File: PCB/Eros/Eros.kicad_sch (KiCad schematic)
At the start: 113 parts, among them IC1 ADS1292RIPBS, J1 USB_C_PowerOnly_6P, J2 UART, J3 Li-ion, J4 Conn_01x08_Socket, J5 AudioJack3, J6 Micro_SD_Card, J7 Conn_01x03_Socket, Q1 BC817, SW1 SW_Push, SW2 SW_Push, SW4 SW_Push, SW5 SW_Push, SW6 SW_SPDT, U1 ESP32-WROOM-32E, U2 LIS3DH, U3 MCP73831-2-OT, U4 AP2112K-3.3, U6 MCP100-315D

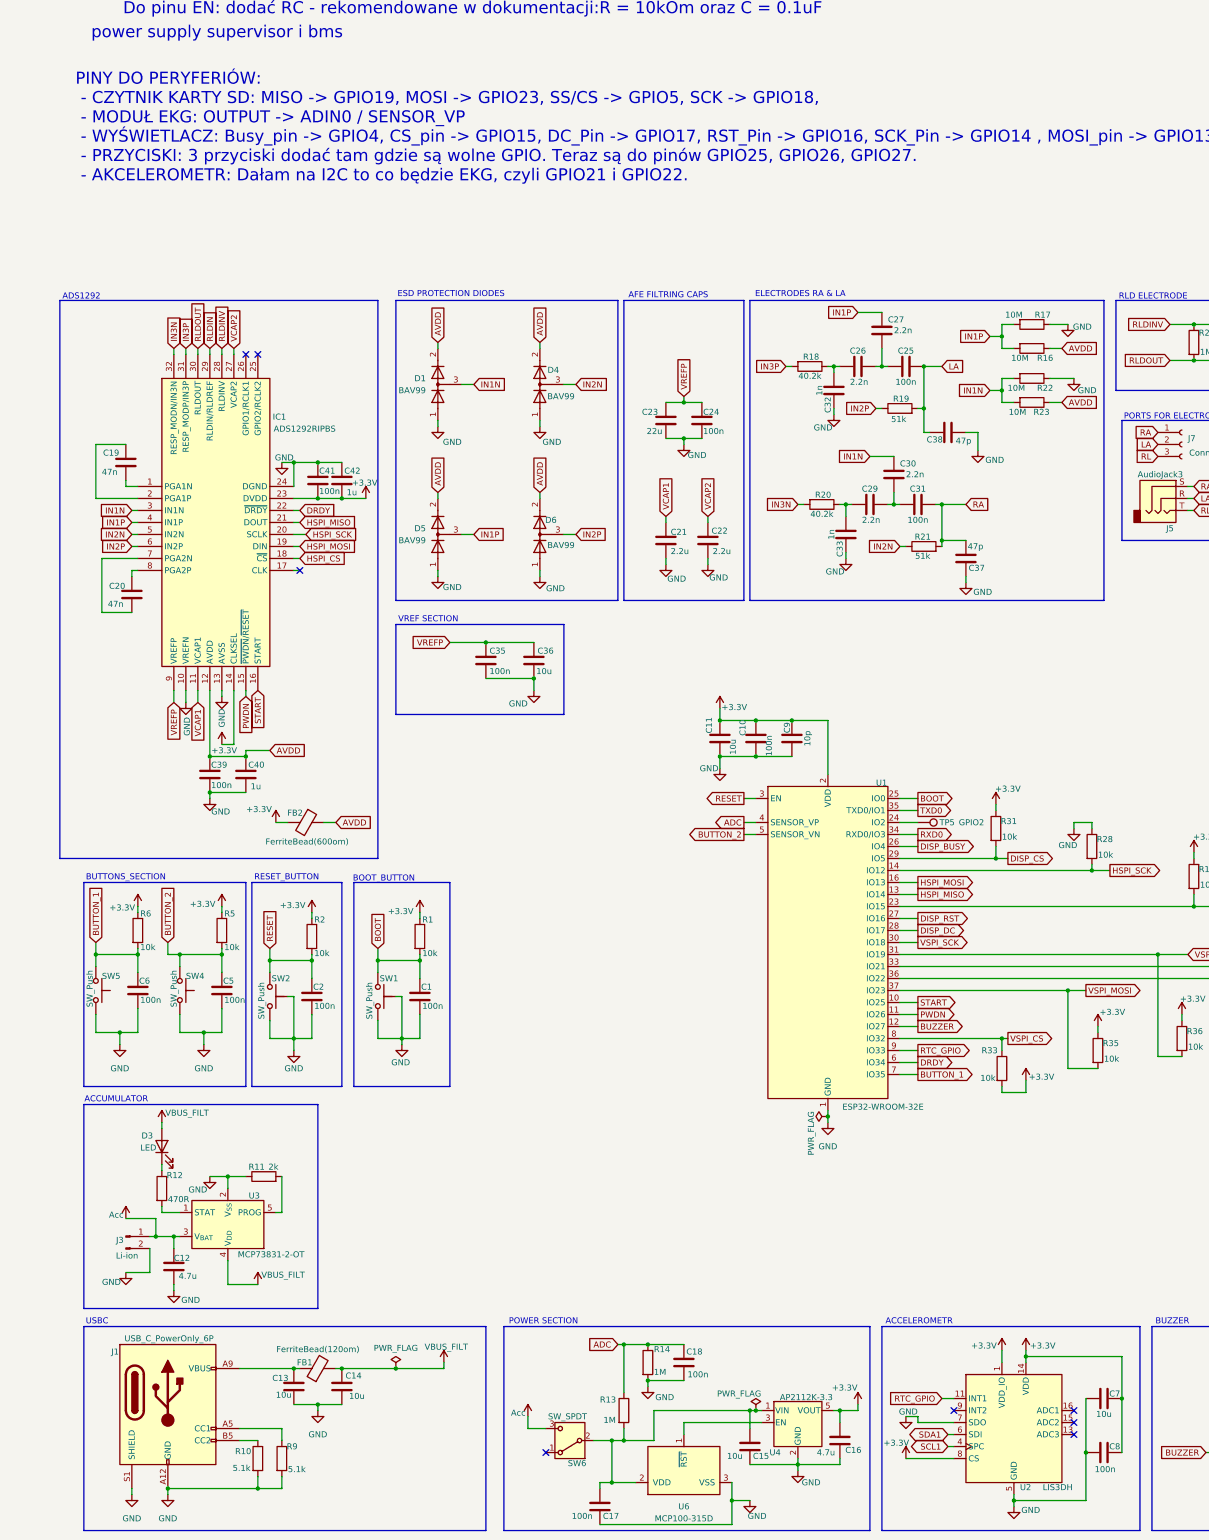
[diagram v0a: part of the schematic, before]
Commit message: poprawa czytelności sekcji zasilania
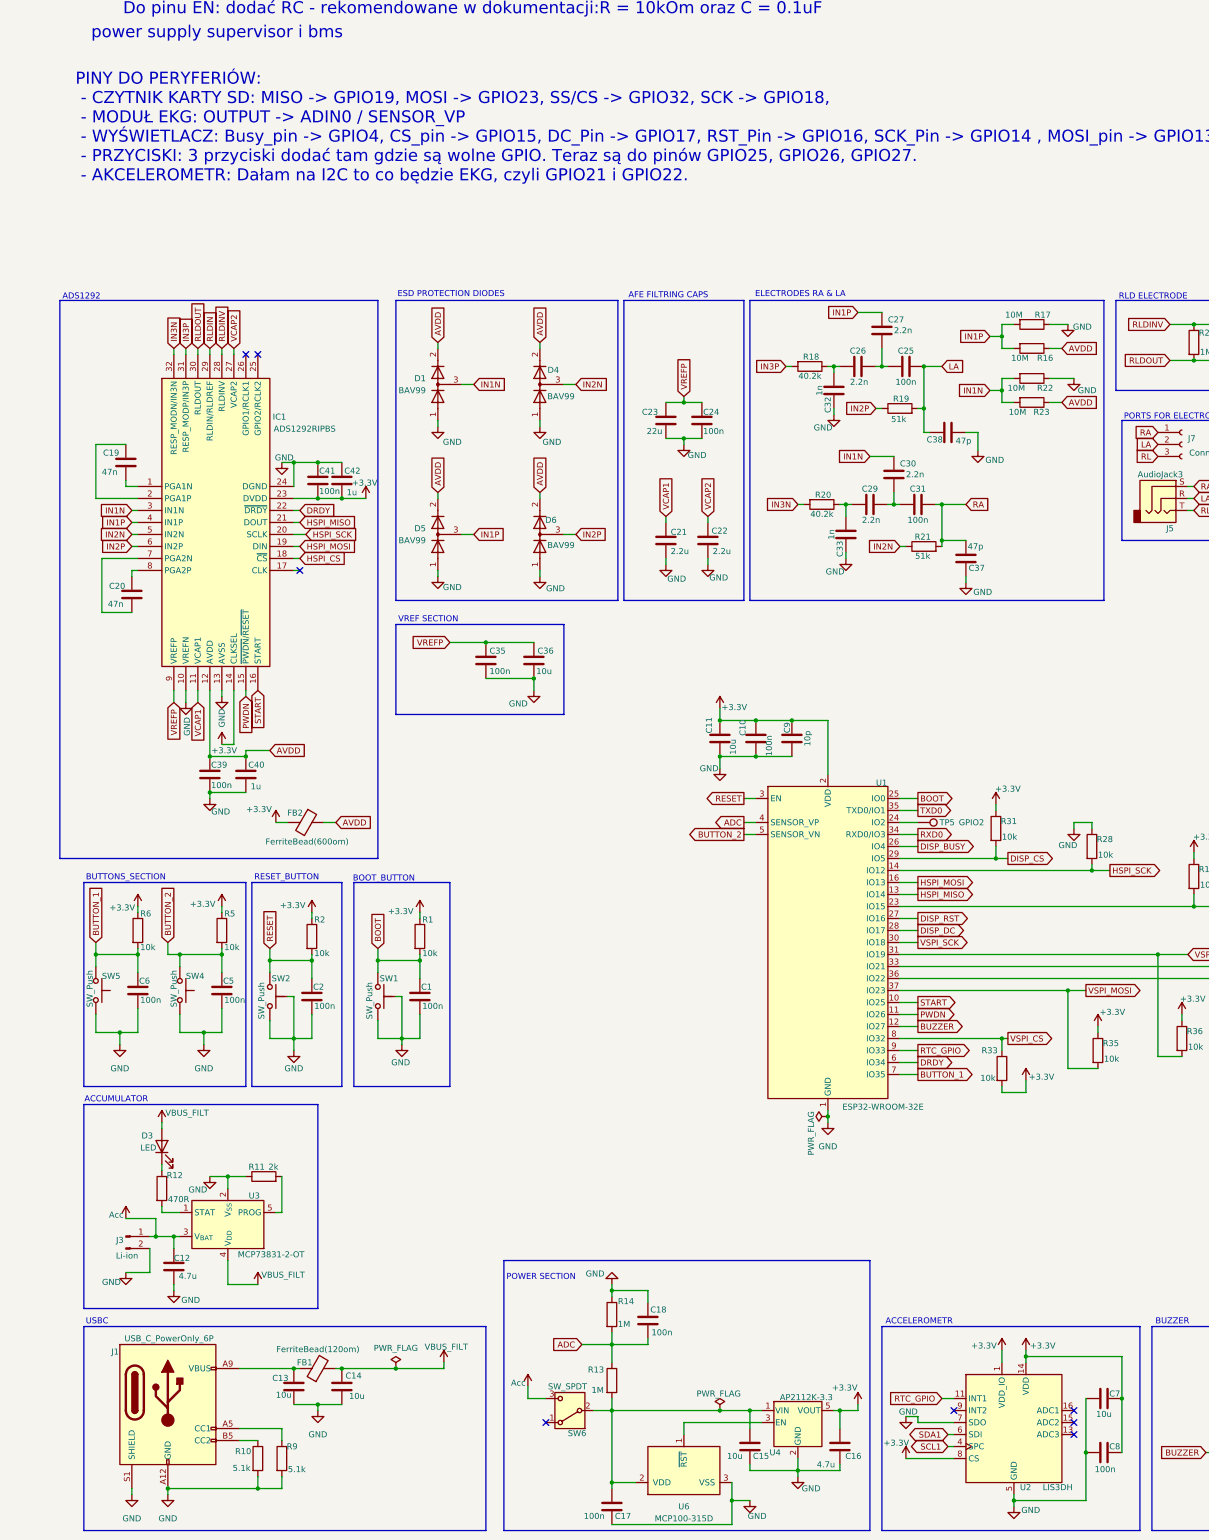
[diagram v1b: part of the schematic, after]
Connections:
- net ADC: now also C18.2, R14.2; no longer C18.1, R14.1
- net GND: now also C18.1, R14.1; no longer C18.2, R14.2
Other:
- note added: "PINY DO PERYFERIÓW: - CZYTNIK KARTY SD: MISO -> GPIO19, MOSI -> GPIO23, SS/CS -> GPIO32, SCK -> GPIO18, - MODUŁ EKG: OUTPUT -> ADIN0 / SENSOR_VP - WYŚWIETLACZ: Busy_pin -> GPIO4, CS_pin -> GPIO15, DC_Pin -> GPIO17, RST_Pin -> GPIO16, SCK_Pin -> GPIO14 , MOSI_pin -> GPIO13; - PRZYCISKI: 3 przyciski dodać tam gdzie są wolne GPIO. Teraz są do pinów GPIO25, GPIO26, GPIO27. - AKCELEROMETR: Dałam na I2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"
- note removed: "PINY DO PERYFERIÓW: - CZYTNIK KARTY SD: MISO -> GPIO19, MOSI -> GPIO23, SS/CS -> GPIO5, SCK -> GPIO18, - MODUŁ EKG: OUTPUT -> ADIN0 / SENSOR_VP - WYŚWIETLACZ: Busy_pin -> GPIO4, CS_pin -> GPIO15, DC_Pin -> GPIO17, RST_Pin -> GPIO16, SCK_Pin -> GPIO14 , MOSI_pin -> GPIO13; - PRZYCISKI: 3 przyciski dodać tam gdzie są wolne GPIO. Teraz są do pinów GPIO25, GPIO26, GPIO27. - AKCELEROMETR: Dałam na I2C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"
- moved on the sheet: C16, C17, C18, R13, R14, SW6

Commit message: zmiana komentarzy na aktualne
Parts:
- removed R33: 10k, Resistor_SMD:R_0402_1005Metric_Pad0.72x0.64mm_HandSolder, symbol Device:R
- added R4: 10k, Resistor_SMD:R_0402_1005Metric_Pad0.72x0.64mm_HandSolder, symbol Device:R
- R37, R38: now fitted
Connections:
- net DISP_CS is gone; now on net VSPI_CS: J4.5 (Pin_5), R31.2, U1.29 (IO5)
- net +3.3V: now also R4.1
- net VSPI_CS: no longer J6.2 (DAT3/CD), U1.8 (IO32)
- new net MICRO_SD_CS: J6.2 (DAT3/CD), R4.2, U1.8 (IO32)
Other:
- note added: "PINY DO PERYFERIÓW: - CZYTNIK KARTY SD: MISO -> GPIO19, MOSI -> GPIO23, SS/CS -> GPIO32, SCK -> GPIO18, - MODUŁ EKG: HSPI - WYŚWIETLACZ: Busy_pin -> GPIO4, CS_pin -> GPIO5, DC_Pin -> GPIO17, RST_Pin -> GPIO16, SCK_Pin -> GPIO18 , MOSI_pin -> GPIO23; - PRZYCISKI: piny GPIO5, GPIO37. - AKCELEROMETR: I2C GPIO21 i GPIO22."
- note removed: "PINY DO PERYFERIÓW: - CZYTNIK KARTY SD: MISO -> GPIO19, MOSI -> GPIO23, SS/CS -> GPIO32, SCK -> GPIO18, - MODUŁ EKG: OUTPUT -> ADIN0 / SENSOR_VP - WYŚWIETLACZ: Busy_pin -> GPIO4, CS_pin -> GPIO15, DC_Pin -> GPIO17, RST_Pin -> GPIO16, SCK_Pin -> GPIO14 , MOSI_pin -> GPIO13; - PRZYCISKI: 3 przyciski dodać tam gdzie są wolne GPIO. Teraz są do pinów GPIO25, GPIO26, GPIO27. - AKCELEROMETR: Dałam na I2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"

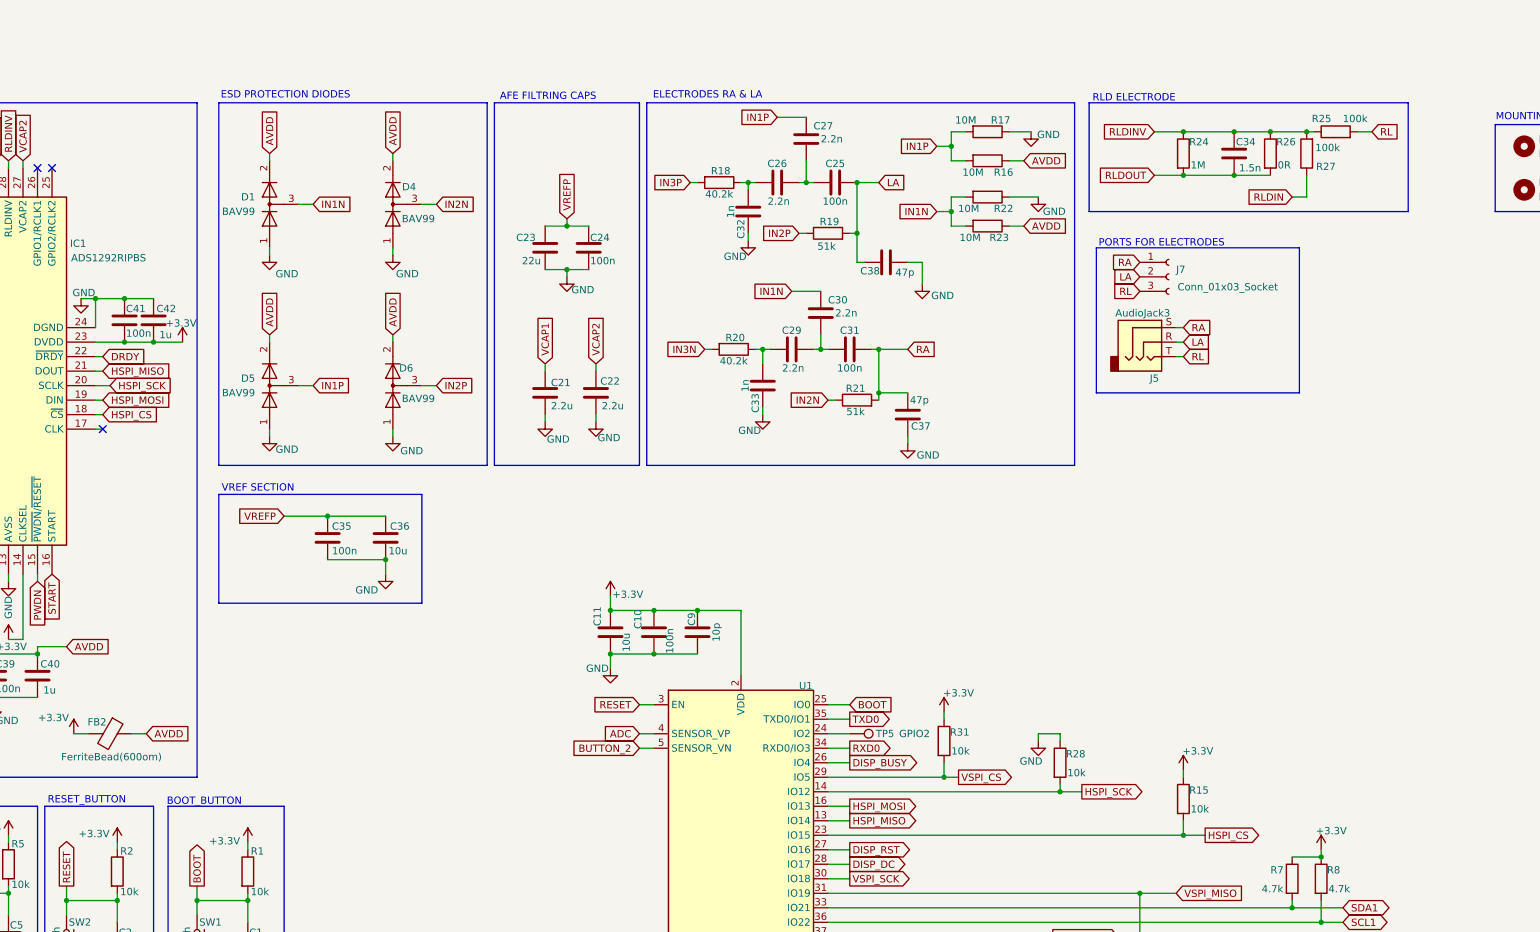
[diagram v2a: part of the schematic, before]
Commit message: poprawa bloku "RLD ELECTRODE"
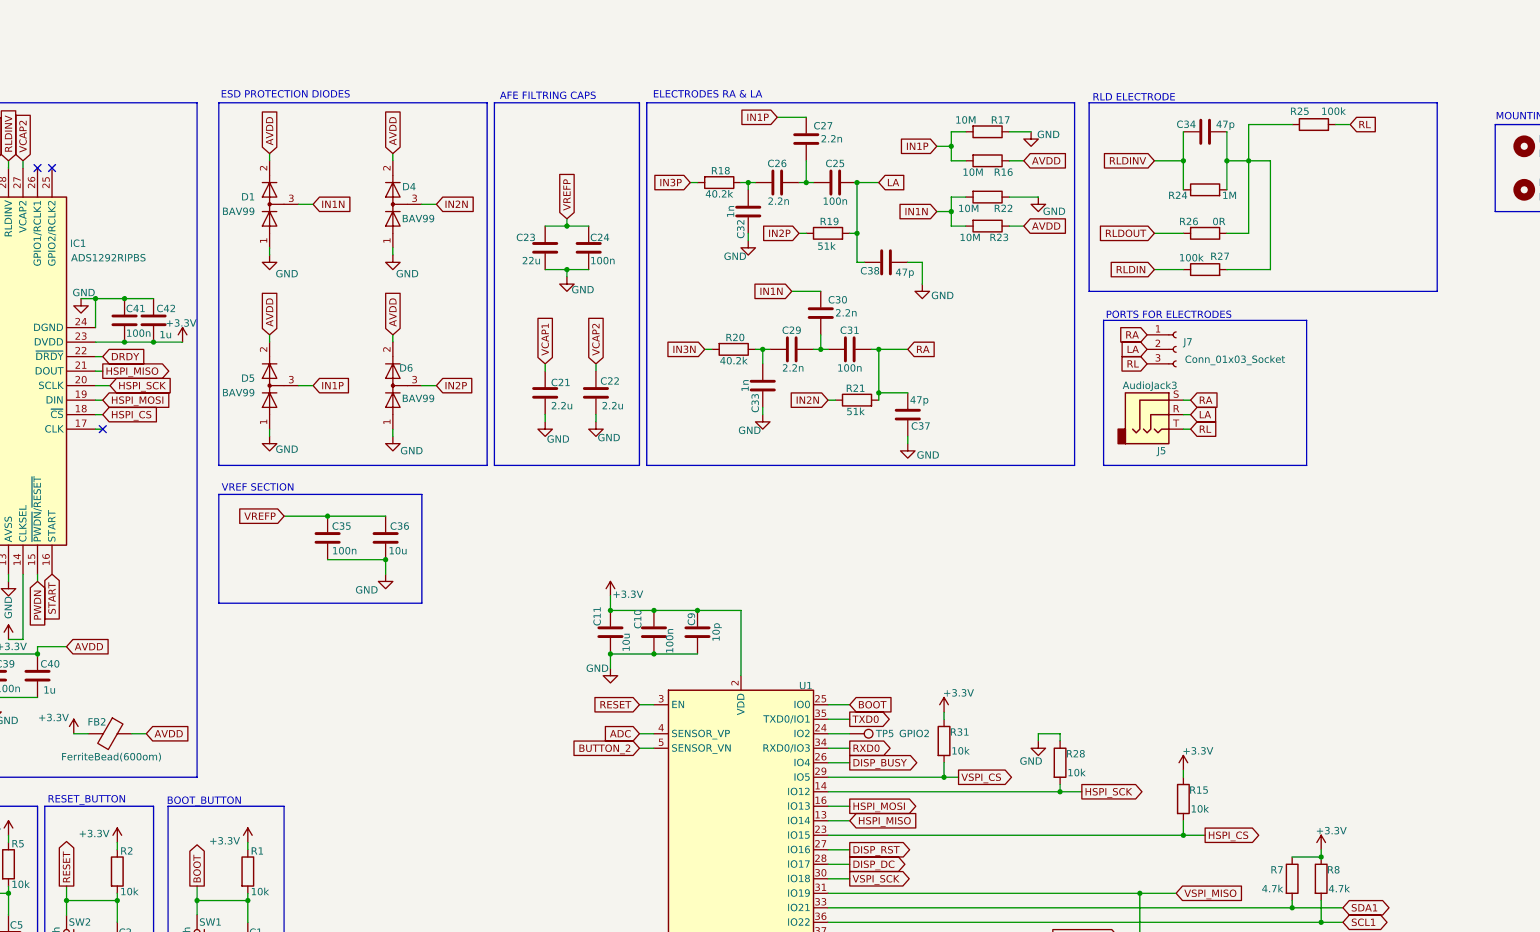
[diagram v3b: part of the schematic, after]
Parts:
- C34: value 1.5n -> 47p
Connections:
- net RLDINV: no longer R25.1, R26.1, R27.2
- net RLDOUT: no longer C34.1, R24.2
- new net: C34.1, R24.2, R25.1, R26.1, R27.2
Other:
- moved on the sheet: C34, J5, J7, R24, R25, R26, R27

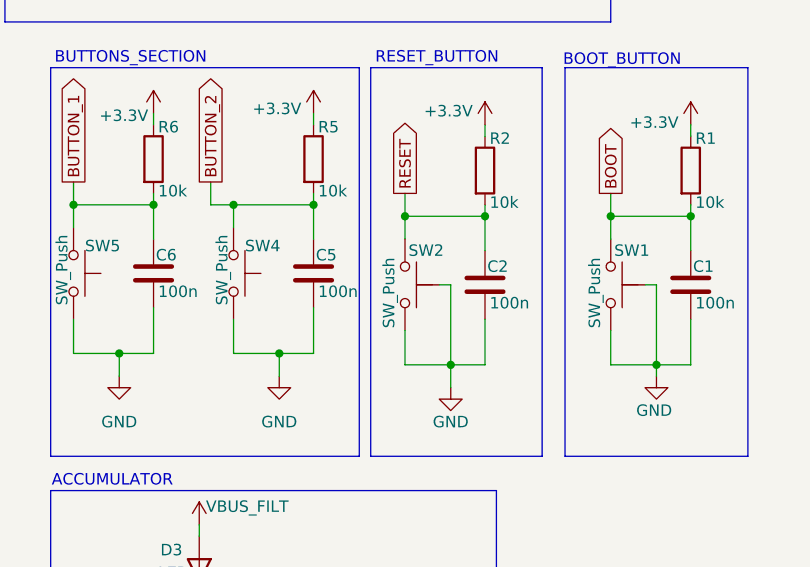
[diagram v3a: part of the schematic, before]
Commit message: podpięcie zasilania
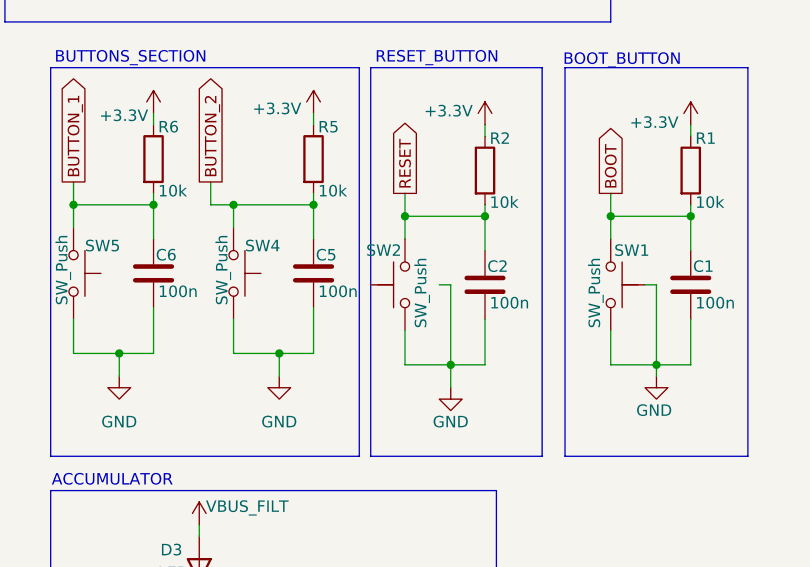
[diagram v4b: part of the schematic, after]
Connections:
- net GND: no longer SW2.SH
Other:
- moved on the sheet: SW2
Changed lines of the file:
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@@
 	(symbol
 		(lib_id "Moje_symbole:SW_Push")
-		(at 58.42 163.83 270)
+		(at 58.42 163.83 90)
+		(mirror x)
 		(unit 1)
 		(exclude_from_sim no)
@@
 		(dnp no)
 		(property "Reference" "SW2"
-			(at 62.738 160.02 90)
+			(at 54.102 160.02 90)
 			(effects
 				(font
@@
 		)
 		(property "Value" "SW_Push"
-			(at 56.642 168.656 0)
+			(at 60.198 168.656 0)
 			(effects
 				(font
@@
 		)
 		(property "Footprint" "Button_Switch_SMD:SW_Push_1P1T-SH_NO_CK_KMR2xxG"
-			(at 63.5 163.83 0)
+			(at 53.34 163.83 0)
 			(effects
 				(font
@@
 		)
 		(property "Datasheet" "~"
-			(at 63.5 163.83 0)
+			(at 53.34 163.83 0)
 			(effects
 				(font

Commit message: Clear Comments, write README.md
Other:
- note added: "Address: 0011000b"
- note removed: "Do pinu EN: dodać RC - rekomendowane w dokumentacji:R = 10kOm oraz C = 0.1uF"
- note removed: "GPIO6-GPIO11 są do pamięci flash, dlatego nie ma ich na schemacie"
- note removed: "Na pin VDD można podpiąć napięcie od 3.0V do 3.6V"
- note removed: "Notatki"
- note removed: "PINY DO PERYFERIÓW: - CZYTNIK KARTY SD: MISO -> GPIO19, MOSI -> GPIO23, SS/CS -> GPIO32, SCK -> GPIO18, - MODUŁ EKG: HSPI - WYŚWIETLACZ: Busy_pin -> GPIO4, CS_pin -> GPIO5, DC_Pin -> GPIO17, RST_Pin -> GPIO16, SCK_Pin -> GPIO18 , MOSI_pin -> GPIO23; - PRZYCISKI: piny GPIO5, GPIO37. - AKCELEROMETR: I2C GPIO21 i GPIO22."
- note removed: "STRAPPING PINS: - GPIO0: do boot; najlepiej podciągnąć do 3.3V przez rezystor 10Kom i dodać przycisk, który ściąga do GND, - GPIO12: najlepiej nie podłączać; jeśli trzeba użyć jako gpio(bo wszystkie inne zajęte) to trzeba się upewnić, że przy starcie nie wymuszany jest stan wysoki, - GPIO2: podczas wchodzenia w tryb programowania, pin musi być w stanie niskim lub niepodłączonym; póżniej już nie m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"
- note removed: "power supply supervisor i bms"
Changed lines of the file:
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@@
 		)
 	)
-	(text "power supply supervisor i bms"
+	(text "Address: 0011000b"
 		(exclude_from_sim no)
-		(at 47.244 -40.132 0)
+		(at 201.93 273.304 0)
 		(effects
 			(font
-				(size 2.54 2.54)
+				(size 1.27 1.27)
 			)
 		)
@@
 		)
 	)
-	(text "PINY DO PERYFERIÓW:\n - CZYTNIK KARTY SD: MISO -> GPIO19, MOSI -> GPIO23, SS/CS -> GPIO32, SCK -> GPIO18, \n - MODUŁ EKG: HSPI\n - WYŚWIETLACZ: Busy_pin -> GPIO4, CS_pin -> GPIO5, DC_Pin -> GPIO17, RST_Pin -> GPIO16, SCK_Pin -> GPIO18 , MOSI_pin -> GPIO23;\n - PRZYCISKI: piny GPIO5, GPIO37.\n - AKCELEROMETR: I2C GPIO21 i GPIO22. "
-		(exclude_from_sim no)
-		(at 17.272 -20.066 0)
-		(effects
-			(font
-				(size 2.54 2.54)
-			)
-			(justify left)
-		)
-	)
 	(text "TEST PADS AND CONNECTIONS"
 		(exclude_from_sim no)
@@
 			)
 			(justify left)
-		)
-	)
-	(text "Notatki"
-		(exclude_from_sim no)
-		(at 27.94 -97.028 0)
-		(effects
-			(font
-				(size 3.81 3.81)
-			)
 		)
 	)
@@
 		)
 	)
-	(text "Do pinu EN: dodać RC - rekomendowane w dokumentacji:R = 10kOm oraz C = 0.1uF"
-		(exclude_from_sim no)
-		(at 101.346 -45.212 0)
-		(effects
-			(font
-				(size 2.54 2.54)
-			)
-		)
-	)
-	(text "Na pin VDD można podpiąć napięcie od 3.0V do 3.6V"
-		(exclude_from_sim no)
-		(at 69.85 -50.546 0)
-		(effects
-			(font
-				(size 2.54 2.54)
-			)
-		)
-	)
 	(text "MICROSD SLOT"
 		(exclude_from_sim no)
@@
 			)
 			(justify left)
-		)
-	)
-	(text "GPIO6-GPIO11 są do pamięci flash, dlatego nie ma ich na schemacie"
-		(exclude_from_sim no)
-		(at 86.614 -88.138 0)
-		(effects
-			(font
-				(size 2.54 2.54)
-			)
 		)
 	)
@@
 		)
 	)
-	(text "STRAPPING PINS:\n - GPIO0: do boot; najlepiej podciągnąć do 3.3V przez rezystor 10Kom i dodać przycisk, który ściąga do GND,\n - GPIO12: najlepiej nie podłączać; jeśli trzeba użyć jako gpio(bo wszystkie inne zajęte) to trzeba się upewnić, że przy starcie nie wymuszany jest stan wysoki,\n - GPIO2: podczas wchodzenia w tryb programowania, pin musi być w stanie niskim lub niepodłączonym; póżniej już nie ma znaczenia jaki ma stan,\n - GPIO15: ma wewnątrz pull-up więc domyślnie jest na 3.3V, można używać jako GPIO; on odpowiada za to, że w trminalu jest boot:0x13 (SPI_FAST_FLASH_BOOT),\ngdy przy włączaniu esp32, będzie na stan 0 to esp32 będzie milczeć podczas startu, na schemacie w dokumentacji nie widać rezystora podciągającego, \nco oznacza że wewnątrz krzemu jest podciągnięcie i one jest bardzo słabe. jak się chce być w 100% pewnym to można podciągnąć go zewnętrznie do 3,3V\n - GPIO5: ma wewnętrzny pull-up, nie ma znaczenia, gdy gpio0 i gpio2 są poprawnie ustawione, unikać urządzeń które przy starcie wymuszają stan niski."
-		(exclude_from_sim no)
-		(at 17.78 -69.088 0)
-		(effects
-			(font
-				(size 2.54 2.54)
-			)
-			(justify left)
-		)
-	)
